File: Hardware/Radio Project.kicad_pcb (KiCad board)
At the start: 2 copper layers, 100 x 100 mm, 4 parts, among them J1 RJ45_Abracon_ARJP11A-MASA-B-A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, U1 Si4464, U2 Si4464, U3 STM32F407VGT6

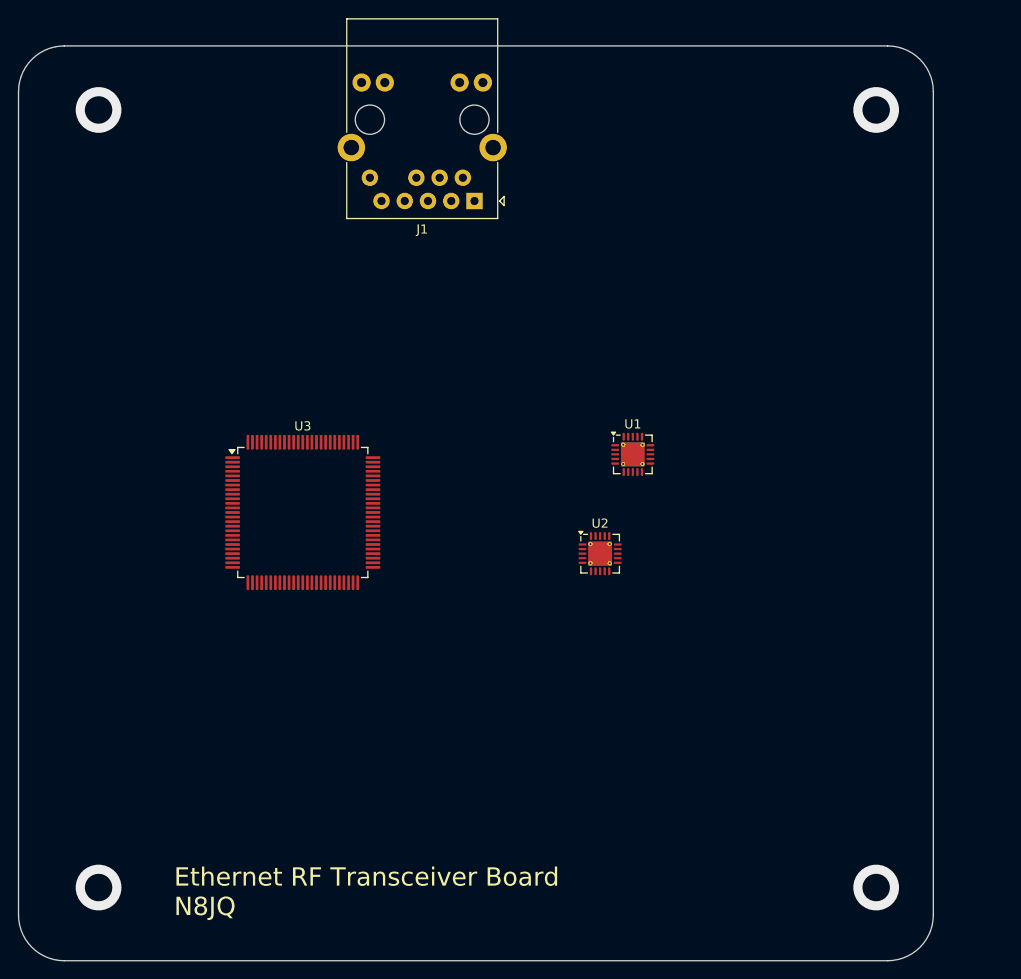
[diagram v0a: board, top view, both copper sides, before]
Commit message: added SWD header and dip switches for boot modes
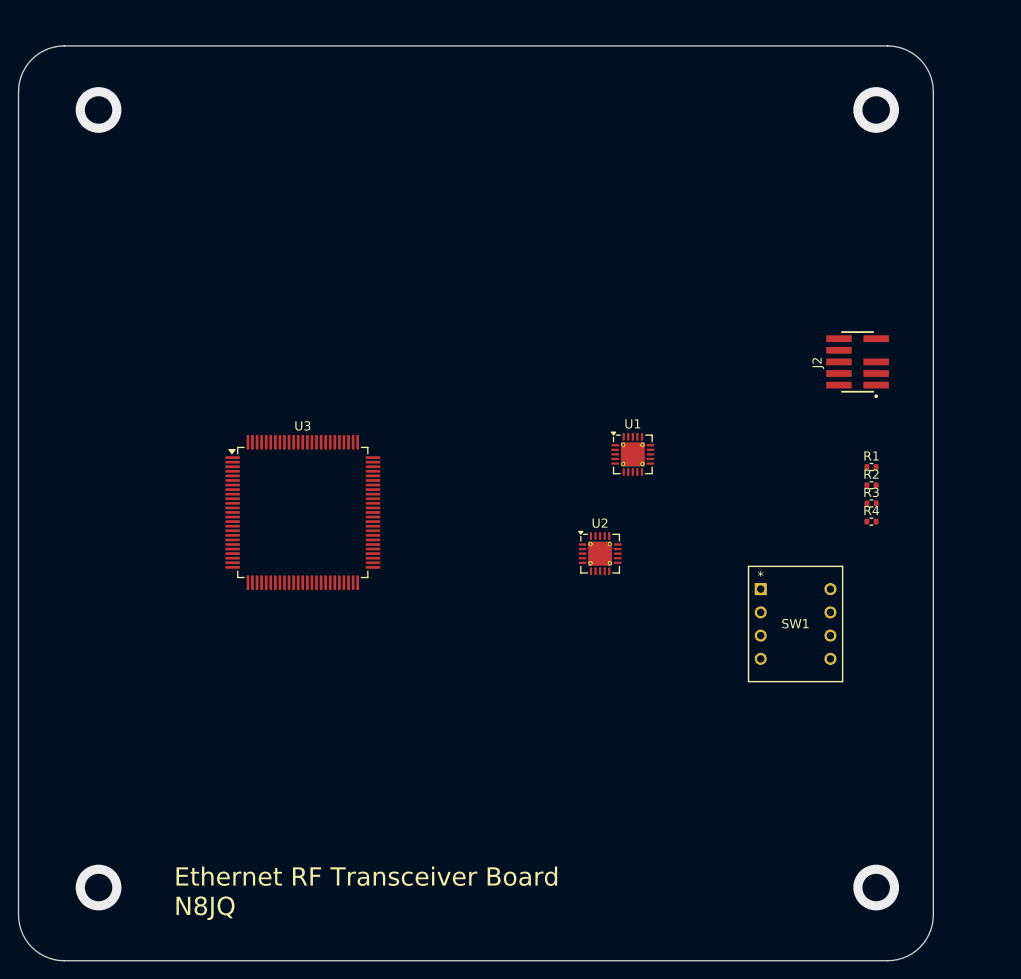
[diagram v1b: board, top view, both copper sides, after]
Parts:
- removed J1: RJ45_Abracon_ARJP11A-MASA-B-A-EMU2, Connector_RJ:RJ45_Abracon_ARJP11A-MA_Horizontal
- added J2: FTSH-105-X-X-DV-007-P-X, FTSH-105-01-L-DV-007-K:SAMTEC_FTSH-105-X-X-DV-007-P-X, F.Cu at (188.0, 82.5)
- added R1: 100k, Resistor_SMD:R_0402_1005Metric, F.Cu at (189.5, 94.0)
- added R2: 100k, Resistor_SMD:R_0402_1005Metric, F.Cu at (189.5, 96.0)
- added R3: 1K, Resistor_SMD:R_0402_1005Metric, F.Cu at (189.5, 98.0)
- added R4: 1K, Resistor_SMD:R_0402_1005Metric, F.Cu at (189.5, 100.0)
- added SW1: 208-4, 208-4:DIP8_208-4_CTS, F.Cu at (177.4, 107.4)
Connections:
- U1 pad 18: Net-(U1-GND-Pad18) -> GND
- U1 pad 21: Net-(U1-GND-Pad18) -> GND
- U2 pad 18: Net-(U2-GND-Pad18) -> GND
- U2 pad 21: Net-(U2-GND-Pad18) -> GND
- U3 pad 14: unconnected-(U3-NRST-Pad14) -> /NRST
- U3 pad 21: unconnected-(U3-VREF+-Pad21) -> +3.3V
- U3 pad 37: unconnected-(U3-PB2-Pad37) -> /Boot1
- U3 pad 72: unconnected-(U3-PA13-Pad72) -> /SWDIO
- U3 pad 76: unconnected-(U3-PA14-Pad76) -> /SWCLK
- U3 pad 89: unconnected-(U3-PB3-Pad89) -> /SWO
- U3 pad 94: unconnected-(U3-BOOT0-Pad94) -> /Boot0
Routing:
- net GND: vias 0 -> 4
- net (no net): vias 4 -> 0
- added copper zone on In2.Cu, net GND
- added copper zone on In4.Cu, net GND
- added copper zone on In5.Cu, net GND
- added copper zone on In7.Cu, net GND
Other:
- copper layers 2 -> 10

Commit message: Added 3.3V power connections and a USB-C connector for +5V
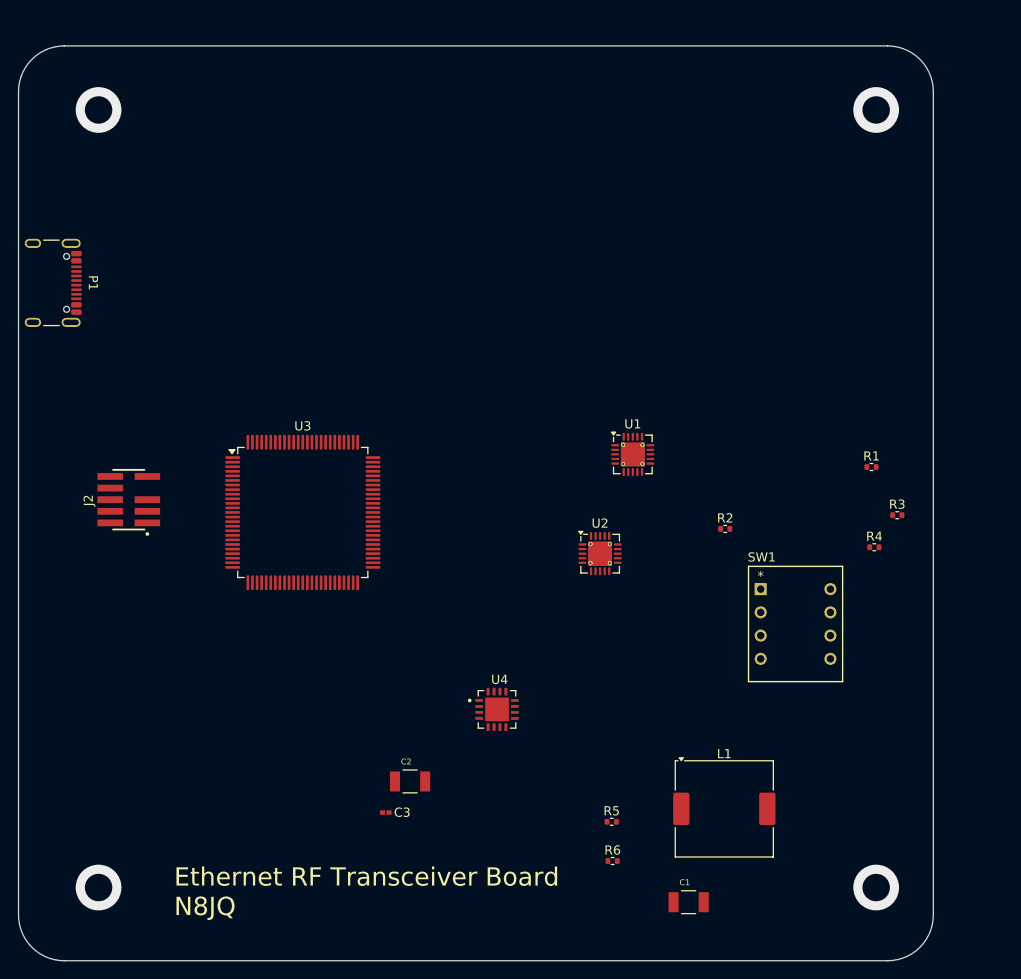
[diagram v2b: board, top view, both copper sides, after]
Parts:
- added C1: 100uF, C3225X5R0J107M250AB:CAP_C3225X5R0J107M250AB, F.Cu at (169.5, 141.6)
- added C2: 47uF, C3225X5R0J476M250AA:CAP_C3225X5R0J476M250AA, F.Cu at (139.1, 128.4)
- added C3: 100nF, C0402C104J8RACTU:CAPC10555_55N_KEM-L, F.Cu at (136.4, 131.8)
- added L1: MSS1038-152NLC, Inductor_SMD:L_Coilcraft_MSS1038-XXX, F.Cu at (173.4, 131.4)
- added P1: USB_C_Plug_USB2.0, Connector_USB:USB_C_Receptacle_GCT_USB4105-xx-A_16P_TopMnt_Horizontal, F.Cu at (98.9, 73.9)
- added R5: 10k, Resistor_SMD:R_0402_1005Metric, F.Cu at (161.1, 132.8)
- added R6: 10, Resistor_SMD:R_0402_1005Metric, F.Cu at (161.2, 137.1)
- added U4: ADP2164ACPZ-3.3-R7, ADP2164ACPZ_3_3_R7:QFN65P400X400X80-17N, F.Cu at (148.6, 120.5)
- moved J2 81.1 mm to (108.3, 97.6)
- moved R2 16.7 mm to (173.5, 100.8)
- moved R3 3.09 mm to (192.3, 99.3)
- moved R4 2.82 mm to (189.8, 102.8)
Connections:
- net /Boot0 renamed Boot0
- net /Boot1 renamed Boot1
- net /NRST renamed NRST
- net /SWCLK renamed SWCLK
- net /SWDCLK renamed SWDCLK
- net /SWDIO renamed SWDIO
- net /SWO renamed SWO

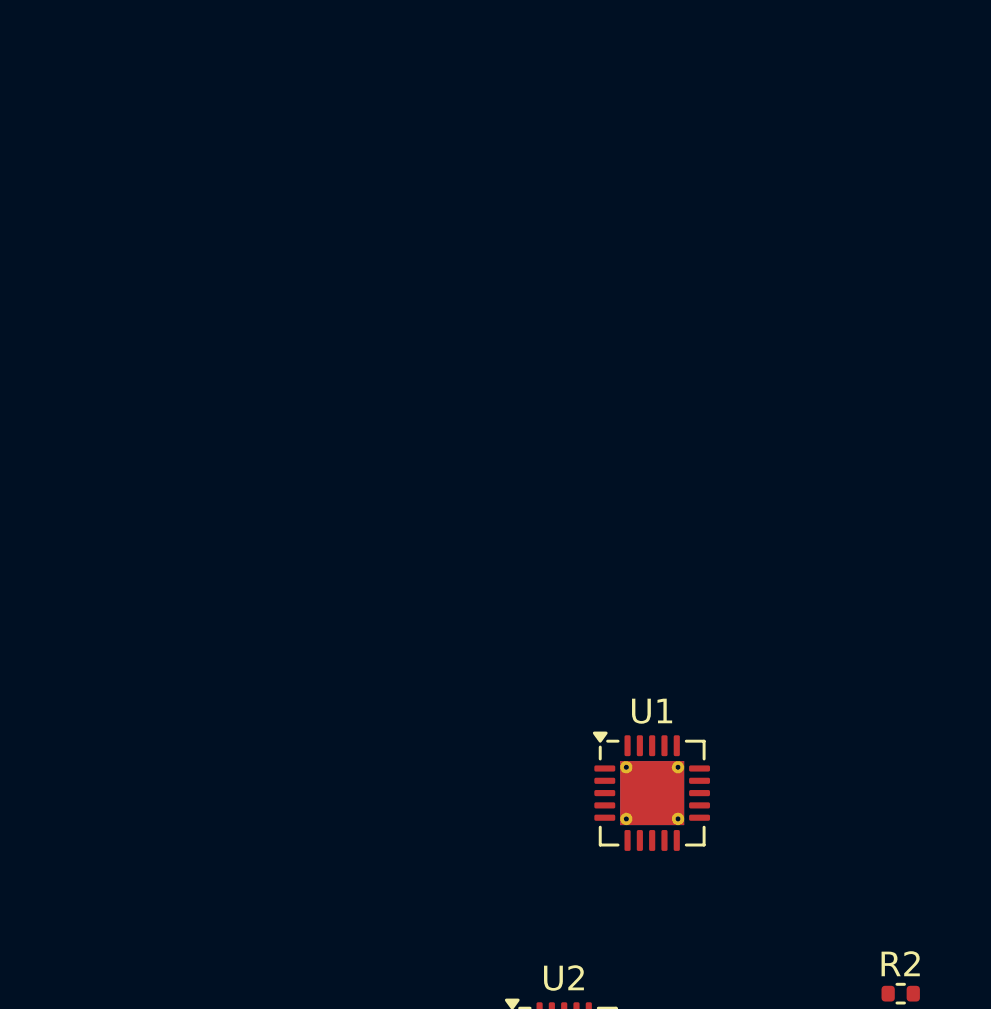
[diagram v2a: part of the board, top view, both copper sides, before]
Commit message: added filtering caps, bulk decoupling caps, and power LED
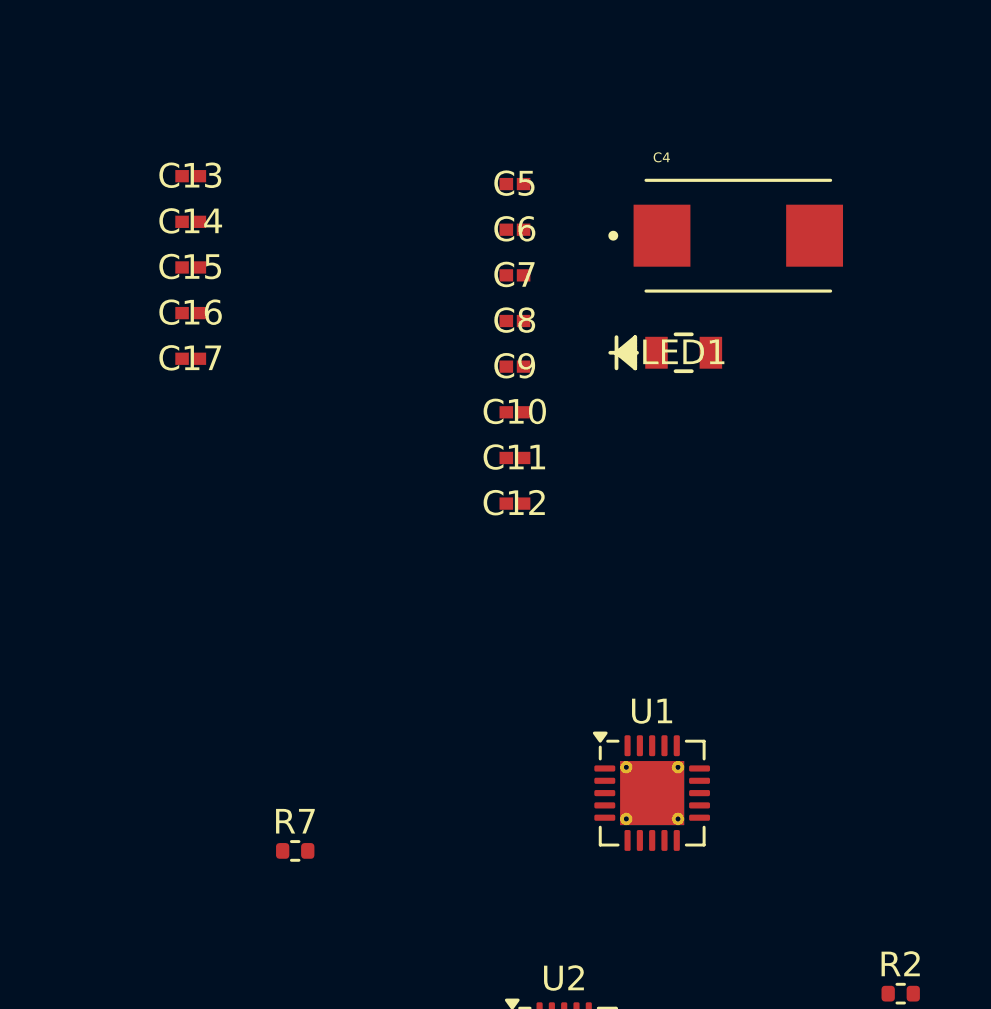
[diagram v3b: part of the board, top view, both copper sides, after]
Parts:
- added C10: 100nF, C0402C104J8RACTU:CAPC10555_55N_KEM-L, F.Cu at (157.8, 77.2)
- added C11: 100nF, C0402C104J8RACTU:CAPC10555_55N_KEM-L, F.Cu at (157.8, 79.0)
- added C12: 100nF, C0402C104J8RACTU:CAPC10555_55N_KEM-L, F.Cu at (157.8, 80.9)
- added C13: 100nF, C0402C104J8RACTU:CAPC10555_55N_KEM-L, F.Cu at (144.6, 67.6)
- added C14: 100nF, C0402C104J8RACTU:CAPC10555_55N_KEM-L, F.Cu at (144.6, 69.4)
- added C15: 100nF, C0402C104J8RACTU:CAPC10555_55N_KEM-L, F.Cu at (144.6, 71.3)
- added C16: 100nF, C0402C104J8RACTU:CAPC10555_55N_KEM-L, F.Cu at (144.6, 73.1)
- added C17: 100nF, C0402C104J8RACTU:CAPC10555_55N_KEM-L, F.Cu at (144.6, 75.0)
- added C4: 330uF, TRME337K010R0035:CAPPM7343X310N, F.Cu at (166.9, 70.0)
- added C5: 100nF, C0402C104J8RACTU:CAPC10555_55N_KEM-L, F.Cu at (157.8, 67.9)
- added C6: 100nF, C0402C104J8RACTU:CAPC10555_55N_KEM-L, F.Cu at (157.8, 69.8)
- added C7: 100nF, C0402C104J8RACTU:CAPC10555_55N_KEM-L, F.Cu at (157.8, 71.6)
- added C8: 100nF, C0402C104J8RACTU:CAPC10555_55N_KEM-L, F.Cu at (157.8, 73.5)
- added C9: 100nF, C0402C104J8RACTU:CAPC10555_55N_KEM-L, F.Cu at (157.8, 75.3)
- added LED1: CMD17-21VGD/TR8, CMD17_21VGD_TR8:LED0805N_CML-M, F.Cu at (164.7, 74.8)
- added R7: 60, Resistor_SMD:R_0402_1005Metric, F.Cu at (148.9, 95.0)

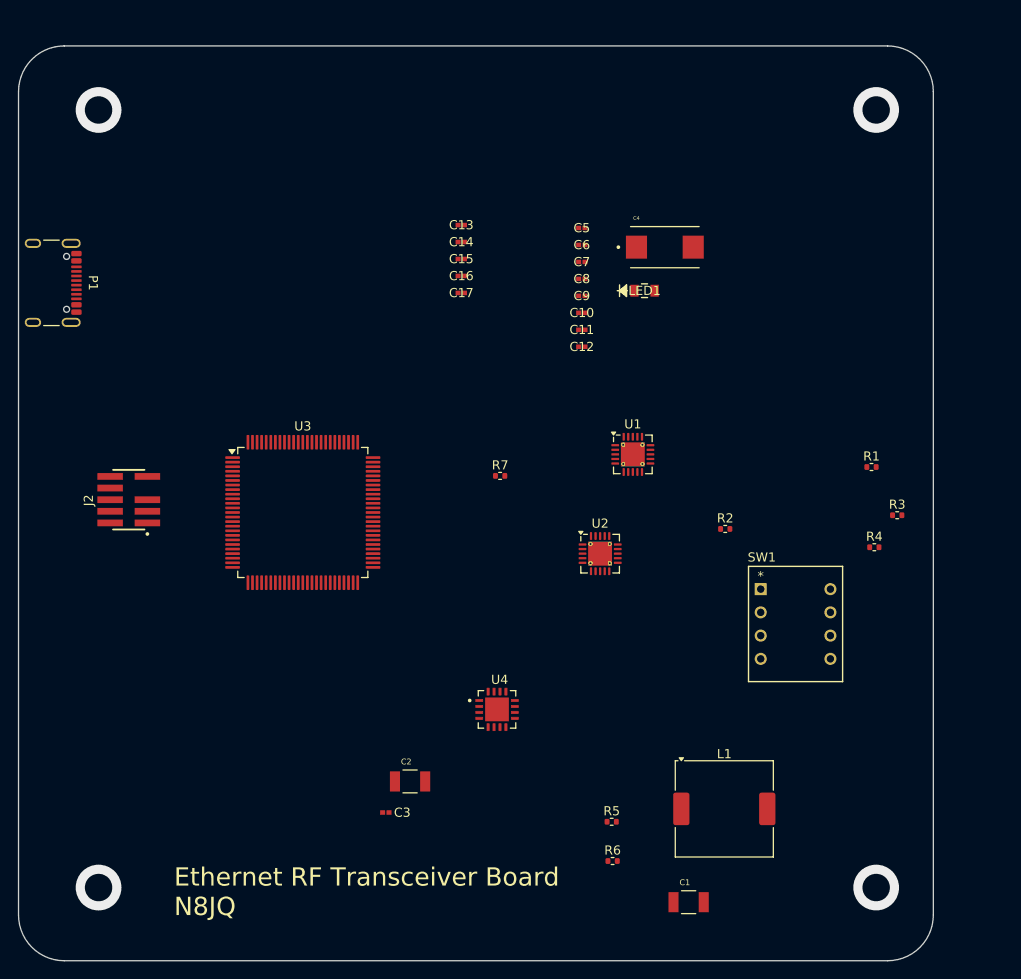
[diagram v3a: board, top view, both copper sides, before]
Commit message: added SMA connectors and external connections sheet
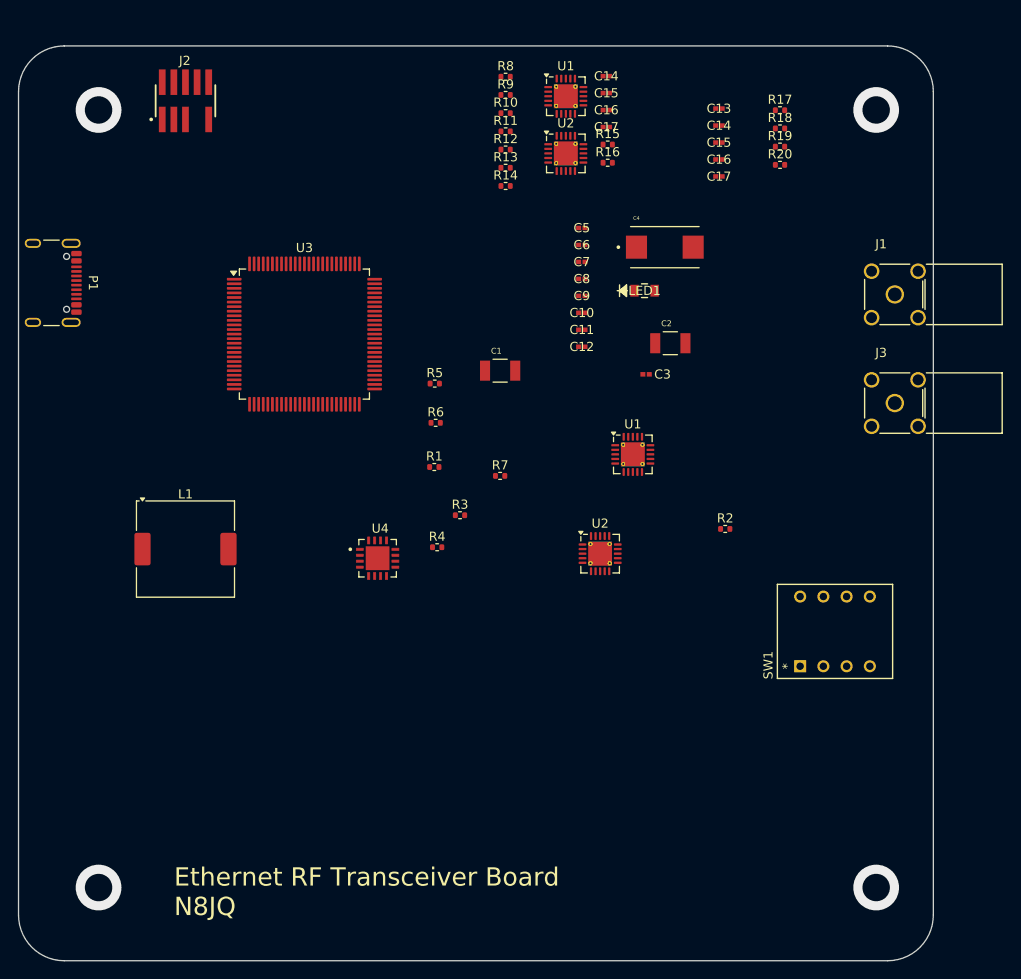
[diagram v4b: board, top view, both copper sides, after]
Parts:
- added C14: 100nF, C0402C104J8RACTU:CAPC10555_55N_KEM-L, F.Cu at (160.5, 51.3)
- added C15: 100nF, C0402C104J8RACTU:CAPC10555_55N_KEM-L, F.Cu at (160.5, 53.2)
- added C16: 100nF, C0402C104J8RACTU:CAPC10555_55N_KEM-L, F.Cu at (160.5, 55.0)
- added C17: 100nF, C0402C104J8RACTU:CAPC10555_55N_KEM-L, F.Cu at (160.5, 56.9)
- added J1: 132225, 132225:CONN_132225_AMP, F.Cu at (192.0, 75.2)
- added J3: 132225, 132225:CONN_132225_AMP, F.Cu at (192.0, 87.0)
- added R10: 40, Resistor_SMD:R_0402_1005Metric, F.Cu at (149.5, 55.4)
- added R11: 40, Resistor_SMD:R_0402_1005Metric, F.Cu at (149.5, 57.3)
- added R12: 40, Resistor_SMD:R_0402_1005Metric, F.Cu at (149.5, 59.3)
- added R13: 40, Resistor_SMD:R_0402_1005Metric, F.Cu at (149.5, 61.3)
- added R14: 40, Resistor_SMD:R_0402_1005Metric, F.Cu at (149.5, 63.3)
- added R15: 40, Resistor_SMD:R_0402_1005Metric, F.Cu at (160.7, 58.8)
- added R16: 40, Resistor_SMD:R_0402_1005Metric, F.Cu at (160.7, 60.8)
- added R17: 40, Resistor_SMD:R_0402_1005Metric, F.Cu at (179.5, 55.0)
- added R18: 40, Resistor_SMD:R_0402_1005Metric, F.Cu at (179.5, 57.0)
- added R19: 40, Resistor_SMD:R_0402_1005Metric, F.Cu at (179.5, 59.0)
- added R20: 40, Resistor_SMD:R_0402_1005Metric, F.Cu at (179.5, 61.0)
- added R8: 40, Resistor_SMD:R_0402_1005Metric, F.Cu at (149.5, 51.4)
- added R9: 40, Resistor_SMD:R_0402_1005Metric, F.Cu at (149.5, 53.4)
- added U1: Si4464, Package_DFN_QFN:QFN-20-1EP_4x4mm_P0.5mm_EP2.6x2.6mm_ThermalVias, F.Cu at (156.1, 53.5)
- added U2: Si4464, Package_DFN_QFN:QFN-20-1EP_4x4mm_P0.5mm_EP2.6x2.6mm_ThermalVias, F.Cu at (156.1, 59.8)
- moved L1 65.4 mm to (114.5, 103.0)
- moved C1 61.6 mm to (148.9, 83.5)
- moved C2 55.7 mm to (167.5, 80.5)
- moved C3 55.7 mm to (164.8, 83.9)
- moved R5 51.7 mm to (141.8, 84.9)
- moved R6 51.7 mm to (141.8, 89.2)
- moved R1 47.8 mm to (141.7, 94.0)
- moved R3 47.8 mm to (144.5, 99.3)
- moved R4 47.8 mm to (142.0, 102.8)
- moved J2 44.0 mm to (114.5, 54.0), turned to 0 degrees
- moved C13 30.9 mm to (172.8, 54.9)
- moved C14 30.9 mm to (172.8, 56.7)
- moved C15 30.9 mm to (172.8, 58.6)
- moved C16 30.9 mm to (172.8, 60.4)
- moved C17 30.9 mm to (172.8, 62.3)
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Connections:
- J2 pad 02: SWDIO -> Net-(J2-Pad02)
- J2 pad 04: SWDCLK -> Net-(J2-Pad04)
- J2 pad 10: NRST -> Net-(J2-Pad10)
- U3 pad 29: unconnected-(U3-PA4-Pad29) -> Net-(U3-PA4)
- U3 pad 30: unconnected-(U3-PA5-Pad30) -> Net-(U3-PA5)
- U3 pad 31: unconnected-(U3-PA6-Pad31) -> RF1_SDO
- U3 pad 32: unconnected-(U3-PA7-Pad32) -> Net-(U3-PA7)
- U3 pad 51: unconnected-(U3-PB12-Pad51) -> Net-(U3-PB12)
- U3 pad 52: unconnected-(U3-PB13-Pad52) -> Net-(U3-PB13)
- U3 pad 53: unconnected-(U3-PB14-Pad53) -> RF2_SDO
- U3 pad 54: unconnected-(U3-PB15-Pad54) -> Net-(U3-PB15)
- U3 pad 72: SWDIO -> Net-(U3-PA13)
- U3 pad 89: SWO -> Net-(U3-PB3)
